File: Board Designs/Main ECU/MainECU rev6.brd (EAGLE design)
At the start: 120.6 x 78.9 mm, 191 parts, among them J1 JUMPER, J2 JUMPER, J3 JUMPER, J4 JUMPER, J5 JUMPER, J6 JUMPER, Q1 P-CHANNEL_MOSFET_DMP3099L-7, Q12 P-CHANNEL_MOSFET_DMP3099L-7, X1 CONNECTOR-37, X2 CONNECTOR-4AUTOSPORT, X3 CONNECTOR-4NANO-FIT-VERTICAL-4, X4 CONNECTOR-4NANO-FIT-VERTICAL-4

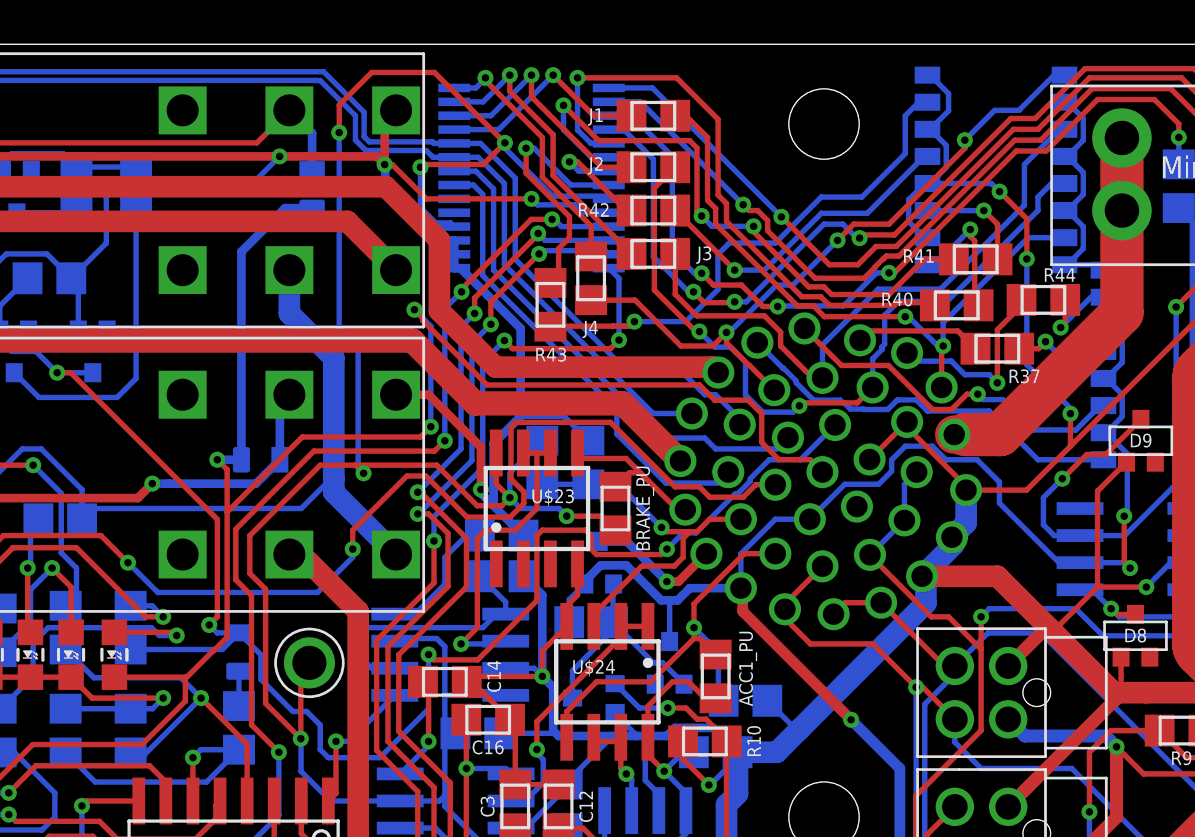
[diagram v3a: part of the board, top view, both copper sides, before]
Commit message: Main ECU rev5/6: Shorten traces, tweak silkscreen
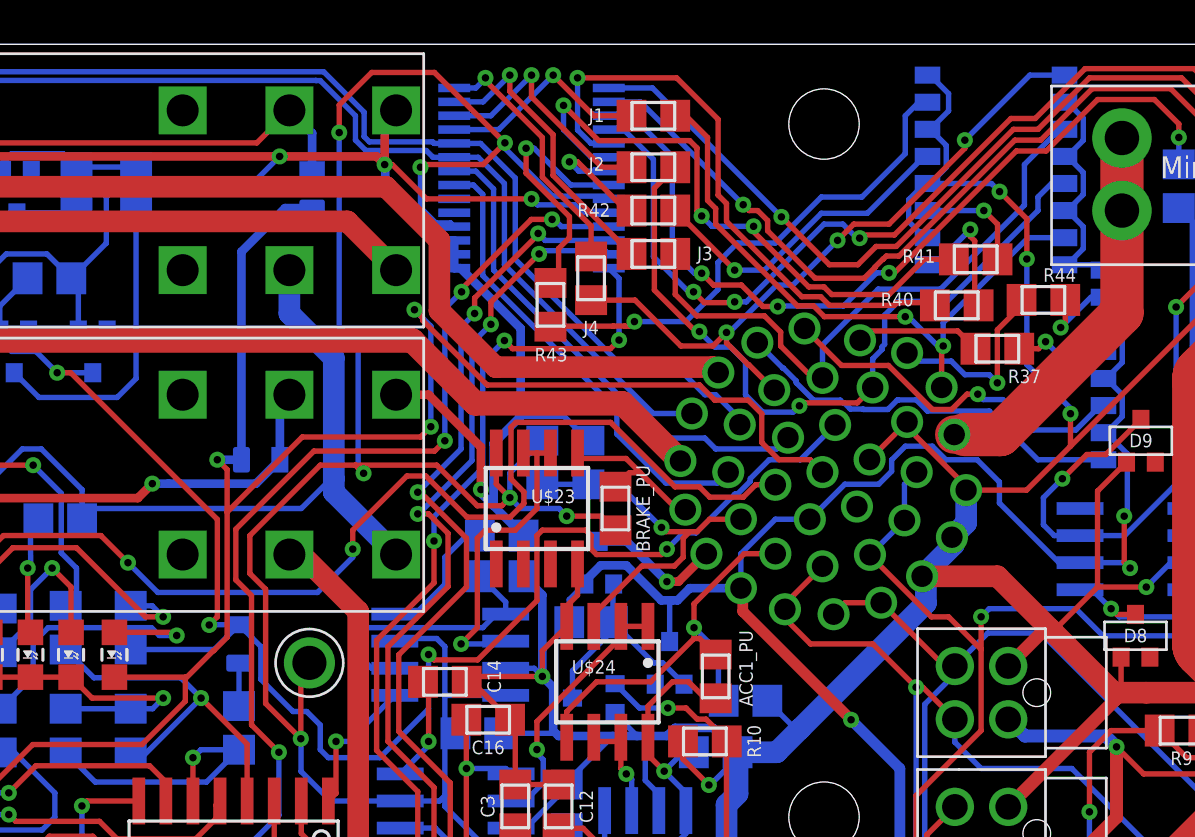
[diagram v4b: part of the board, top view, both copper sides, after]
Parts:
- moved D2 0.38 mm to (42.4, 50.8)
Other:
- board text added: "HyTech 2019 Main ECU rev6"
- board text removed: "HyTech 2019 Main ECU rev5"
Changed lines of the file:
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@@
 <grid distance="5" unitdist="mil" unit="mil" style="lines" multiple="1" display="yes" altdistance="5" altunitdist="mil" altunit="mil"/>
 <layers>
-<layer number="1" name="Top" color="4" fill="1" visible="no" active="yes"/>
+<layer number="1" name="Top" color="4" fill="1" visible="yes" active="yes"/>
 <layer number="2" name="Route2" color="16" fill="1" visible="no" active="no"/>
 <layer number="3" name="Route3" color="17" fill="1" visible="no" active="no"/>
@@
 <layer number="19" name="Unrouted" color="6" fill="1" visible="yes" active="yes"/>
 <layer number="20" name="Dimension" color="24" fill="1" visible="yes" active="yes"/>
-<layer number="21" name="tPlace" color="7" fill="1" visible="no" active="yes"/>
+<layer number="21" name="tPlace" color="7" fill="1" visible="yes" active="yes"/>
 <layer number="22" name="bPlace" color="7" fill="1" visible="yes" active="yes"/>
-<layer number="23" name="tOrigins" color="15" fill="1" visible="no" active="yes"/>
+<layer number="23" name="tOrigins" color="15" fill="1" visible="yes" active="yes"/>
 <layer number="24" name="bOrigins" color="15" fill="1" visible="yes" active="yes"/>
-<layer number="25" name="tNames" color="7" fill="1" visible="no" active="yes"/>
+<layer number="25" name="tNames" color="7" fill="1" visible="yes" active="yes"/>
 <layer number="26" name="bNames" color="7" fill="1" visible="yes" active="yes"/>
 <layer number="27" name="tValues" color="7" fill="1" visible="no" active="yes"/>
@@
 <layer number="37" name="tTest" color="7" fill="1" visible="no" active="yes"/>
 <layer number="38" name="bTest" color="7" fill="1" visible="no" active="yes"/>
-<layer number="39" name="tKeepout" color="4" fill="11" visible="no" active="yes"/>
+<layer number="39" name="tKeepout" color="4" fill="11" visible="yes" active="yes"/>
 <layer number="40" name="bKeepout" color="1" fill="11" visible="yes" active="yes"/>
-<layer number="41" name="tRestrict" color="4" fill="10" visible="no" active="yes"/>
+<layer number="41" name="tRestrict" color="4" fill="10" visible="yes" active="yes"/>
 <layer number="42" name="bRestrict" color="1" fill="10" visible="yes" active="yes"/>
 <layer number="43" name="vRestrict" color="2" fill="10" visible="no" active="yes"/>
@@
 <layer number="49" name="Reference" color="7" fill="1" visible="no" active="yes"/>
 <layer number="50" name="dxf" color="7" fill="1" visible="no" active="no"/>
-<layer number="51" name="tDocu" color="7" fill="1" visible="no" active="yes"/>
+<layer number="51" name="tDocu" color="7" fill="1" visible="yes" active="yes"/>
 <layer number="52" name="bDocu" color="7" fill="1" visible="yes" active="yes"/>
 <layer number="53" name="tGND_GNDA" color="7" fill="9" visible="no" active="no"/>
@@
 <rectangle x1="18.9865" y1="5.7785" x2="19.3675" y2="5.8547" layer="51"/>
 <rectangle x1="20.5105" y1="5.7785" x2="20.9677" y2="5.8547" layer="51"/>
-<text x="24.638" y="3.81" size="1.397" layer="51" font="vector">HyTech 2019 Main ECU rev5</text>
+<text x="24.638" y="3.81" size="1.397" layer="51" font="vector">HyTech 2019 Main ECU rev6</text>
 <text x="24.638" y="2.032" size="1.397" layer="51" font="vector">Designed by Parker Jones</text>
 <text x="32.258" y="48.387" size="0.8128" layer="51" font="vector" rot="R270">Shutdown B</text>
@@
 <attribute name="VALUE" x="14.5288" y="69.8754" size="0.3048" layer="28" font="vector" rot="MR90" align="top-center"/>
 </element>
-<element name="D2" library="HyTechDevices" package="0805_D" value="TS4148 RYG" x="42.418" y="50.419" smashed="yes" rot="MR270">
-<attribute name="NAME" x="41.4401" y="50.419" size="0.635" layer="26" font="vector" rot="MR270" align="bottom-center"/>
-<attribute name="VALUE" x="43.1292" y="50.419" size="0.3048" layer="28" font="vector" rot="MR270" align="top-center"/>
+<element name="D2" library="HyTechDevices" package="0805_D" value="TS4148 RYG" x="42.418" y="50.8" smashed="yes" rot="MR270">
+<attribute name="NAME" x="41.4401" y="50.546" size="0.635" layer="26" font="vector" rot="MR270" align="bottom-center"/>
+<attribute name="VALUE" x="43.1292" y="50.8" size="0.3048" layer="28" font="vector" rot="MR270" align="top-center"/>
 </element>
 <element name="D3" library="HyTechDevices" package="0805_D" value="TS4148 RYG" x="17.653" y="73.279" smashed="yes" rot="MR180">
@@
 <wire x1="59.182" y1="54.991" x2="62.23" y2="54.991" width="0.254" layer="1"/>
 <contactref element="R56" pad="1"/>
-<wire x1="42.418" y1="51.319" x2="41.391" y2="51.319" width="0.254" layer="16"/>
-<wire x1="41.391" y1="51.319" x2="41.021" y2="51.689" width="0.254" layer="16"/>
-<wire x1="37.338" y1="50.537" x2="41.636" y2="50.537" width="0.254" layer="16"/>
-<wire x1="41.636" y1="50.537" x2="42.418" y2="51.319" width="0.254" layer="16"/>
-<wire x1="42.418" y1="51.319" x2="43.4395" y2="50.2975" width="0.254" layer="16"/>
+<wire x1="42.418" y1="51.7" x2="41.032" y2="51.7" width="0.254" layer="16"/>
+<wire x1="41.021" y1="51.689" x2="41.032" y2="51.7" width="0.254" layer="16"/>
+<wire x1="37.338" y1="50.537" x2="41.255" y2="50.537" width="0.254" layer="16"/>
+<wire x1="41.255" y1="50.537" x2="42.418" y2="51.7" width="0.254" layer="16"/>
+<wire x1="42.418" y1="51.7" x2="43.4395" y2="50.6785" width="0.254" layer="16"/>
 <contactref element="Q2" pad="1"/>
 <contactref element="D18" pad="3"/>
@@
 <wire x1="34.528" y1="63.516" x2="33.893" y2="63.516" width="0.254" layer="1"/>
 <via x="33.893" y="63.516" extent="1-16" drill="0.35"/>
-<wire x1="43.4395" y1="50.2975" x2="43.4395" y2="49.1435" width="0.254" layer="16"/>
+<wire x1="43.4395" y1="50.6785" x2="43.4395" y2="49.1435" width="0.254" layer="16"/>
 <wire x1="44.9525" y1="47.6305" x2="45.593" y2="47.6305" width="0.254" layer="16"/>
 <wire x1="43.4395" y1="49.1435" x2="44.9525" y2="47.6305" width="0.254" layer="16"/>
@@
 <contactref element="R7" pad="1"/>
 <contactref element="D2" pad="C"/>
-<wire x1="42.418" y1="49.519" x2="42.418" y2="47.888" width="0.254" layer="16"/>
+<wire x1="42.418" y1="49.9" x2="42.418" y2="47.888" width="0.254" layer="16"/>
 </signal>
 <signal name="N$33">
@@
 <wire x1="63.373" y1="65.913" x2="64.8744" y2="67.4144" width="0.254" layer="16"/>
 <wire x1="69.723" y1="71.755" x2="67.564" y2="69.596" width="0.254" layer="16"/>
-<wire x1="65.405" y1="69.596" x2="67.564" y2="69.596" width="0.254" layer="16"/>
-<wire x1="64.8744" y1="69.0654" x2="65.405" y2="69.596" width="0.254" layer="16"/>
-<wire x1="64.8744" y1="67.4144" x2="64.8744" y2="69.0654" width="0.254" layer="16"/>
+<wire x1="65.786" y1="69.596" x2="67.564" y2="69.596" width="0.254" layer="16"/>
+<wire x1="64.8744" y1="68.6844" x2="65.786" y2="69.596" width="0.254" layer="16"/>
+<wire x1="64.8744" y1="67.4144" x2="64.8744" y2="68.6844" width="0.254" layer="16"/>
 </signal>
 <signal name="DASH_IO8">
@@
 <wire x1="66.3214375" y1="63.893403125" x2="66.29681875" y2="63.893403125" width="0.254" layer="1"/>
 <contactref element="U$30" pad="9"/>
-<wire x1="81.128" y1="77.47" x2="80.645" y2="77.47" width="0.254" layer="16"/>
-<wire x1="80.645" y1="77.47" x2="78.994" y2="75.819" width="0.254" layer="16"/>
 <wire x1="58.928" y1="66.92" x2="60.988921875" y2="66.92" width="0.254" layer="1"/>
-<wire x1="78.994" y1="75.819" x2="77.851" y2="75.819" width="0.254" layer="16"/>
-<wire x1="77.851" y1="75.819" x2="76.454" y2="74.422" width="0.254" layer="16"/>
 <via x="76.454" y="74.422" extent="1-16" drill="0.35"/>
 <wire x1="76.454" y1="74.422" x2="76.454" y2="74.041" width="0.254" layer="1"/>
@@
 <wire x1="65.278" y1="64.912221875" x2="65.278" y2="65.405" width="0.254" layer="1"/>
 <wire x1="66.29681875" y1="63.893403125" x2="65.278" y2="64.912221875" width="0.254" layer="1"/>
+<wire x1="81.128" y1="77.47" x2="79.502" y2="77.47" width="0.254" layer="16"/>
+<wire x1="79.502" y1="77.47" x2="76.454" y2="74.422" width="0.254" layer="16"/>
 </signal>
 <signal name="DASH_CTRL8_OUT">
